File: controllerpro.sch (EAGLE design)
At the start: 10 parts, among them IC1 MCP1703CB, IC2 741G3157DBVR, IC3 741G3157DBVR, IC4 741G3157DBVR, IC5 741G3157DBVR

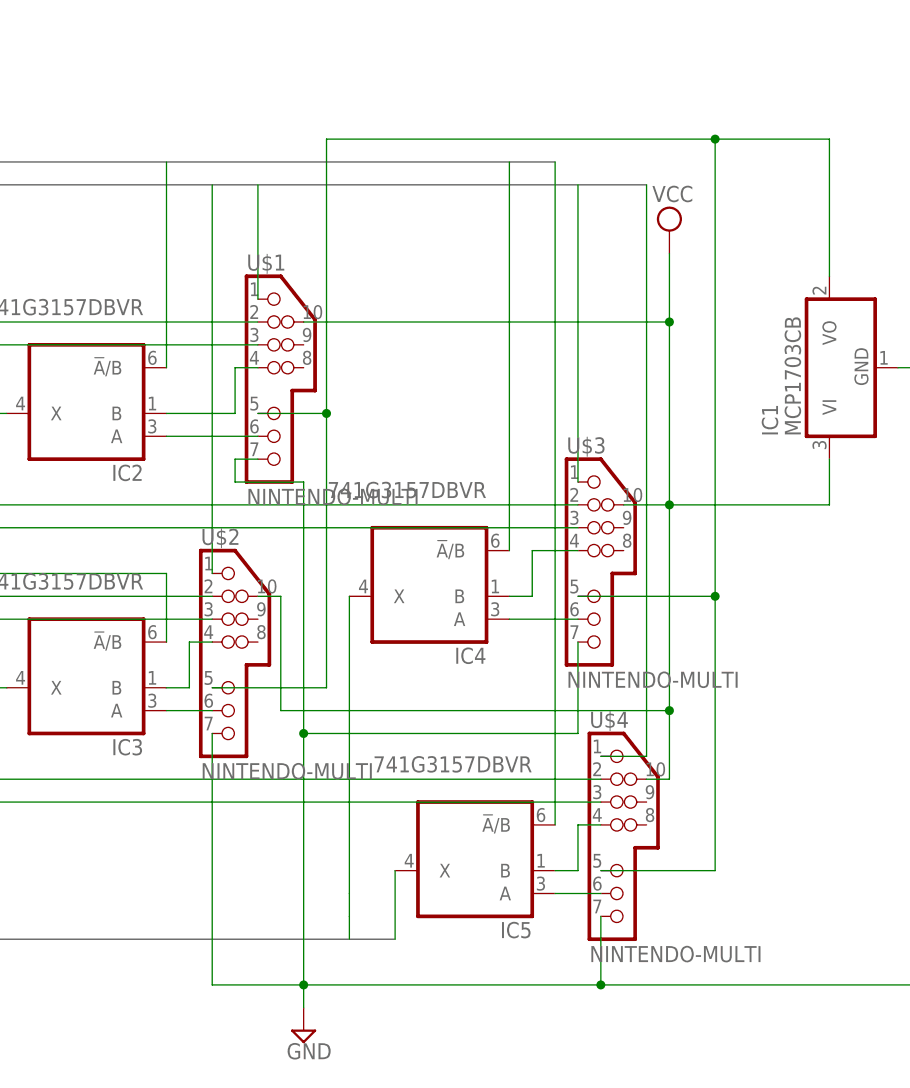
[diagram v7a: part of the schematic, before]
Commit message: Adding pull-up resistors
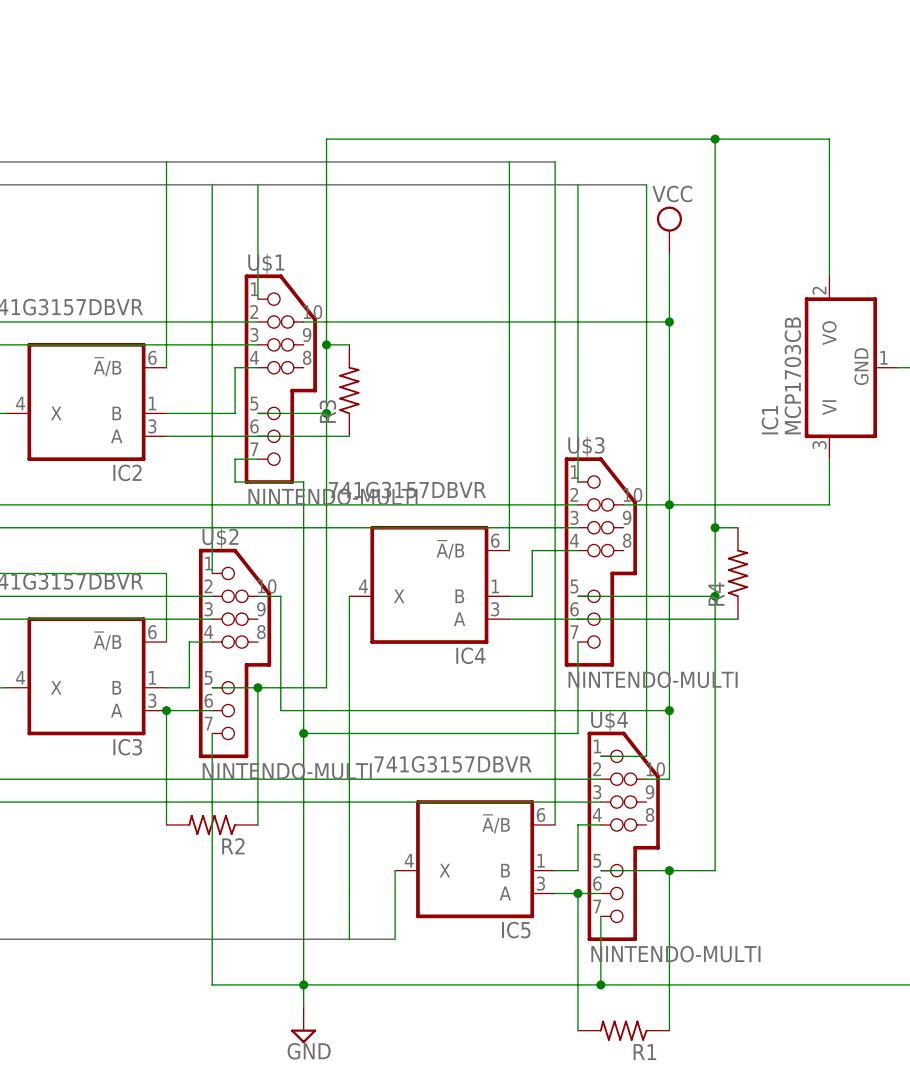
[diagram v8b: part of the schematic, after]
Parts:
- added R1, R2, R3, R4: (no value), rcl:R-US_R0603
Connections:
- net N$12: now also R2.2
- net N$14: now also R4.1
- net N$7: now also R1.2
- net N$8: now also R3.1
- net V33: now also R1.1, R2.1, R3.2, R4.2
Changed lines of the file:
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@@
 <part name="U$5" library="custom" deviceset="TEENSY_MC_PINS" device=""/>
 <part name="SUPPLY6" library="supply2" deviceset="GND" device=""/>
+<part name="R1" library="rcl" deviceset="R-US_" device="R0603"/>
+<part name="R2" library="rcl" deviceset="R-US_" device="R0603"/>
+<part name="R3" library="rcl" deviceset="R-US_" device="R0603"/>
+<part name="R4" library="rcl" deviceset="R-US_" device="R0603"/>
 </parts>
 <sheets>
@@
 <instance part="U$5" gate="G$1" x="53.34" y="53.34" rot="R180"/>
 <instance part="SUPPLY6" gate="GND" x="66.04" y="15.24"/>
+<instance part="R1" gate="G$1" x="160.02" y="15.24" rot="R180"/>
+<instance part="R2" gate="G$1" x="114.3" y="38.1" rot="R180"/>
+<instance part="R3" gate="G$1" x="129.54" y="86.36" rot="R90"/>
+<instance part="R4" gate="G$1" x="172.72" y="66.04" rot="R90"/>
 </instances>
 <busses>
@@
 <segment>
 <wire x1="170.18" y1="114.3" x2="127" y2="114.3" width="0.1524" layer="91"/>
-<wire x1="127" y1="114.3" x2="127" y2="83.82" width="0.1524" layer="91"/>
+<wire x1="127" y1="114.3" x2="127" y2="91.44" width="0.1524" layer="91"/>
 <pinref part="U$2" gate="G$1" pin="5"/>
+<wire x1="127" y1="91.44" x2="127" y2="83.82" width="0.1524" layer="91"/>
 <wire x1="127" y1="83.82" x2="127" y2="53.34" width="0.1524" layer="91"/>
-<wire x1="127" y1="53.34" x2="114.3" y2="53.34" width="0.1524" layer="91"/>
+<wire x1="127" y1="53.34" x2="119.38" y2="53.34" width="0.1524" layer="91"/>
 <pinref part="U$1" gate="G$1" pin="5"/>
+<wire x1="119.38" y1="53.34" x2="114.3" y2="53.34" width="0.1524" layer="91"/>
 <wire x1="119.38" y1="83.82" x2="127" y2="83.82" width="0.1524" layer="91"/>
-<wire x1="170.18" y1="114.3" x2="170.18" y2="63.5" width="0.1524" layer="91"/>
+<wire x1="170.18" y1="114.3" x2="170.18" y2="71.12" width="0.1524" layer="91"/>
 <pinref part="U$3" gate="G$1" pin="5"/>
+<wire x1="170.18" y1="71.12" x2="170.18" y2="63.5" width="0.1524" layer="91"/>
 <wire x1="170.18" y1="63.5" x2="154.94" y2="63.5" width="0.1524" layer="91"/>
 <pinref part="U$4" gate="G$1" pin="5"/>
-<wire x1="157.48" y1="33.02" x2="170.18" y2="33.02" width="0.1524" layer="91"/>
+<wire x1="157.48" y1="33.02" x2="165.1" y2="33.02" width="0.1524" layer="91"/>
+<wire x1="165.1" y1="33.02" x2="170.18" y2="33.02" width="0.1524" layer="91"/>
 <wire x1="170.18" y1="33.02" x2="170.18" y2="63.5" width="0.1524" layer="91"/>
 <junction x="170.18" y="63.5"/>
@@
 <wire x1="182.88" y1="114.3" x2="170.18" y2="114.3" width="0.1524" layer="91"/>
 <junction x="170.18" y="114.3"/>
+<pinref part="R3" gate="G$1" pin="2"/>
+<wire x1="129.54" y1="91.44" x2="127" y2="91.44" width="0.1524" layer="91"/>
+<pinref part="R2" gate="G$1" pin="1"/>
+<wire x1="119.38" y1="38.1" x2="119.38" y2="53.34" width="0.1524" layer="91"/>
+<junction x="119.38" y="53.34"/>
+<junction x="127" y="91.44"/>
+<pinref part="R1" gate="G$1" pin="1"/>
+<wire x1="165.1" y1="33.02" x2="165.1" y2="15.24" width="0.1524" layer="91"/>
+<pinref part="R4" gate="G$1" pin="2"/>
+<wire x1="172.72" y1="71.12" x2="170.18" y2="71.12" width="0.1524" layer="91"/>
+<junction x="170.18" y="71.12"/>
+<junction x="165.1" y="33.02"/>
 </segment>
 </net>
@@
 <pinref part="IC5" gate="G$1" pin="A"/>
 <pinref part="U$4" gate="G$1" pin="6"/>
-<wire x1="152.4" y1="30.48" x2="157.48" y2="30.48" width="0.1524" layer="91"/>
+<wire x1="152.4" y1="30.48" x2="154.94" y2="30.48" width="0.1524" layer="91"/>
+<pinref part="R1" gate="G$1" pin="2"/>
+<wire x1="154.94" y1="30.48" x2="157.48" y2="30.48" width="0.1524" layer="91"/>
+<wire x1="154.94" y1="15.24" x2="154.94" y2="30.48" width="0.1524" layer="91"/>
+<junction x="154.94" y="30.48"/>
 </segment>
 </net>
@@
 <pinref part="U$1" gate="G$1" pin="6"/>
 <wire x1="109.22" y1="81.28" x2="119.38" y2="81.28" width="0.1524" layer="91"/>
+<pinref part="R3" gate="G$1" pin="1"/>
+<wire x1="119.38" y1="81.28" x2="129.54" y2="81.28" width="0.1524" layer="91"/>
 </segment>
 </net>
@@
 <pinref part="U$2" gate="G$1" pin="6"/>
 <wire x1="109.22" y1="50.8" x2="114.3" y2="50.8" width="0.1524" layer="91"/>
+<pinref part="R2" gate="G$1" pin="2"/>
+<wire x1="109.22" y1="38.1" x2="109.22" y2="50.8" width="0.1524" layer="91"/>
+<junction x="109.22" y="50.8"/>
 </segment>
 </net>
@@
 <pinref part="U$3" gate="G$1" pin="6"/>
 <wire x1="147.32" y1="60.96" x2="154.94" y2="60.96" width="0.1524" layer="91"/>
-</segment>
-</net>
+<pinref part="R4" gate="G$1" pin="1"/>
+<wire x1="154.94" y1="60.96" x2="172.72" y2="60.96" width="0.1524" layer="91"/>
+</segment>
+</net>
